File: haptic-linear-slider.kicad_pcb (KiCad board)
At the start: 2 copper layers, 130.5 x 46 mm, 67 parts, among them J1 EXT_CTRL, J2 SWD, J3 USB_C_Receptacle_USB2.0_16P, J4 TBC05-02-1-G-G, SW1 SW_Reset, SW2 SW_Boot, U1 STM32C071KBT6, U2 PSM01-081A-103B2, U3 USBLC6-2SC6, U4 DRV8876PWPR, U5 DIO54335TST6, U6 TLV61048DBVR, U7 TPS22918DBVR

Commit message: review of main components
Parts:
- removed C21: 47u, Capacitor_SMD:C_1210_3225Metric_Pad1.33x2.70mm_HandSolder
- added R10: 1k, Resistor_SMD:R_0805_2012Metric_Pad1.20x1.40mm_HandSolder, F.Cu at (316.2, 214.5)
- added R27: 10k, Resistor_SMD:R_0805_2012Metric_Pad1.20x1.40mm_HandSolder, F.Cu at (226.5, 212.7)
- C9: value 1u -> 10u; footprint Capacitor_SMD:C_0805_2012Metric_Pad1.18x1.45mm_HandSolder -> Capacitor_SMD:C_1210_3225Metric_Pad1.33x2.70mm_HandSolder
- moved D4 27.7 mm to (278.5, 217.6), turned to 180 degrees
- moved R26 21.8 mm to (274.2, 217.6), turned to 0 degrees
- moved C1 14.6 mm to (302.6, 225.9), turned to 0 degrees
- moved C2 13.9 mm to (302.6, 229.5)
- moved C38 13.7 mm to (234.1, 227.8), turned to 90 degrees
- moved C9 10.9 mm to (317.0, 221.1), turned to -90 degrees
- moved D1 10.6 mm to (302.6, 222.8)
- moved R1 10.4 mm to (307.8, 232.4), turned to 90 degrees
- moved C33 8.78 mm to (228.5, 215.2), turned to 0 degrees
- moved U6 7.59 mm to (309.1, 224.7)
- moved R2 7.30 mm to (308.8, 229.2), turned to 0 degrees
- moved J1 6.39 mm to (237.7, 235.1)
- moved C6 6.32 mm to (291.2, 223.2)
- moved U5 5.80 mm to (291.1, 226.6), turned to -90 degrees
- moved R14 5.39 mm to (231.3, 219.0), turned to 180 degrees
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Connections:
- net /LS_CT renamed Net-(U7-CT)
- net /LS_ON renamed Net-(U7-ON)
- net /MOTOR_OUT1 renamed Net-(U4-OUT1)
- net /MOTOR_OUT2 renamed Net-(U4-OUT2)
- C33 pad 1: /MOTOR_VREF_PWM -> Net-(U4-VREF)
- R15 pad 1: /MOTOR_VREF_PWM -> Net-(U4-VREF)
- U4 pad 5: /MOTOR_VREF_PWM -> Net-(U4-VREF)
- U7 pad 5: unconnected-(U7-QOD-Pad5) -> Net-(U7-QOD)
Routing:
- net /CC_SENSE: track 152.9 -> 110.9 mm
- net /POT_WIPER1: track 114.9 -> 78.1 mm, vias 0 -> 1
- net /POT_WIPER2: track 105.6 -> 71.1 mm, vias 0 -> 1
- net Net-(U4-VREF): track 0.00 -> 19.4 mm
- net /MOTOR_VREF_PWM: track 77.0 -> 61.4 mm
- net +10V: track 111.0 -> 121.3 mm
- net Net-(U5-BS): track 2.09 -> 11.4 mm
- net /BOOST_SW: track 9.02 -> 0.00 mm
- net GND: track 82.0 -> 90.3 mm, vias 47 -> 51
- net /TOUCH_SENSE: track 46.4 -> 40.6 mm
- net +5V: track 181.3 -> 175.8 mm
- net Net-(U4-OUT1): track 20.8 -> 15.4 mm
- net /MOTOR_IPROPI: track 64.8 -> 60.4 mm
- net Net-(U4-OUT2): track 17.0 -> 12.6 mm
- net /BUCK_SW: track 8.65 -> 12.5 mm
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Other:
- board text removed: "7 VREF 8 IPRO 9 W1 10 W2 11 TCH 12 CC 13/14 GND"
- board text removed: "J1 EXT CTRL 1 3V3 2 5V 3 IN1 4 IN2 5 SLP 6 FLT"

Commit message: ready to order
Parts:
- removed R6: 1k, Resistor_SMD:R_0805_2012Metric_Pad1.20x1.40mm_HandSolder
- removed SW1: SW_Reset, _Footprints:434133025816
- C17: value 3n3 -> 22n
- J2: footprint Connector_PinHeader_2.54mm:PinHeader_1x04_P2.54mm_Vertical -> Connector_PinHeader_2.54mm:PinHeader_1x05_P2.54mm_Vertical
- U1: value STM32C071KBT6 -> STM32C071KBT3
- moved C2 73.8 mm to (228.9, 235.3), turned to -90 degrees
- moved C10 8.96 mm to (258.9, 229.3), turned to 0 degrees
- moved C38 2.71 mm to (233.5, 225.2), turned to 0 degrees
- moved D3 0.94 mm to (261.7, 202.8), turned to 0 degrees
- moved D2 0.91 mm to (265.9, 202.8), turned to 180 degrees
- moved C36 0.88 mm to (222.6, 232.9)
- moved C37 0.26 mm to (229.2, 231.5)
- moved C11 0.05 mm to (321.6, 215.3)
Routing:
- net GND: track 90.3 -> 60.5 mm, vias 51 -> 47
- net /NRST: track 42.6 -> 34.9 mm
- net Net-(R6-Pad1): track 6.78 -> 0.00 mm
- net Net-(U2-T): track 87.3 -> 93.0 mm
- net /+5V_MOT: track 20.4 -> 15.8 mm
- net +10V: track 121.3 -> 118.8 mm
- net Net-(D3-A): track 2.23 -> 3.11 mm
- net Net-(D2-A): track 2.23 -> 3.09 mm
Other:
- board text added: "+"
- board text added: "-"
- board text added: "3V3"
- board text added: "5V"
- board text added: "CC_SENSE"
- board text added: "GND"
- board text added: "M_IN1"
- board text added: "M_IN2"
- board text added: "M_IPROPI"
- board text added: "M_VREF"
- board text added: "M_~{FAULT}"
- board text added: "M_~{SLEEP}"
- board text added: "NRST"
- board text added: "P_WIPER1"
- board text added: "P_WIPER2"
- board text added: "SWCLK"
- board text added: "SWD"
- board text added: "TC_SENSE"

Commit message: logo
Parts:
- added TP1: TestPoint, TestPoint:TestPoint_THTPad_D1.0mm_Drill0.5mm, F.Cu at (304.2, 231.6)
- moved C23 0.24 mm to (253.8, 214.5)
- moved C22 0.22 mm to (256.3, 214.5)
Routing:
- net /NRST: track 34.9 -> 32.4 mm
- net +10V: track 118.8 -> 120.9 mm
- net GND: track 60.5 -> 61.8 mm
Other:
- board text added: "haptic-linear-slider v1.0.1"

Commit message: v.1.1.0: differential pair size and JCLPCB rules
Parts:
- moved J2 6.54 mm to (289.1, 212.7), turned to 180 degrees
- moved C15 4.55 mm to (281.0, 206.8)
- moved R8 4.55 mm to (278.5, 206.8)
- moved R9 4.55 mm to (283.4, 206.8)
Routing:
- net Net-(J2-Pin_4): track 17.0 -> 5.95 mm, vias 1 -> 0
- net /SWCLK: track 36.8 -> 26.1 mm, vias 1 -> 0
- net /SWD: track 28.9 -> 22.6 mm, vias 1 -> 0
- net /NRST: track 32.4 -> 27.9 mm
- net /USB_D+: track 83.4 -> 84.7 mm
- net /USB_D-: track 84.9 -> 85.6 mm
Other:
- board text added: "haptic-linear-slider v1.1.0"
- board text removed: "haptic-linear-slider v1.0.1"

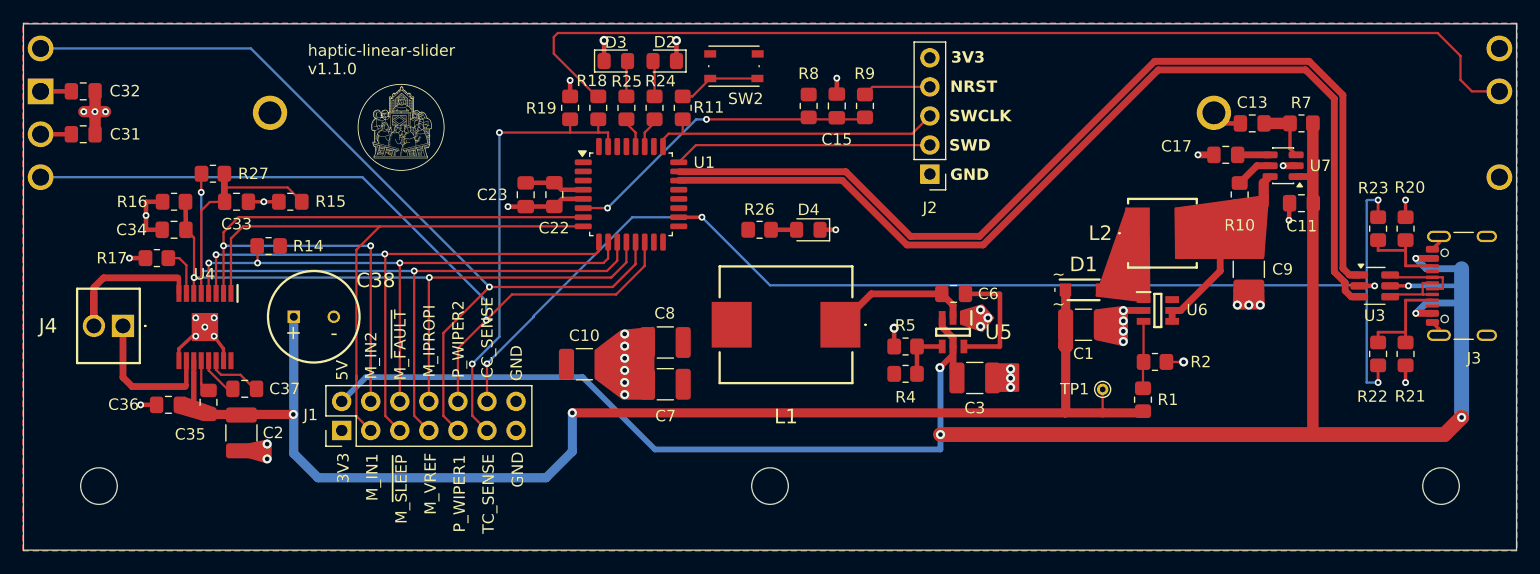
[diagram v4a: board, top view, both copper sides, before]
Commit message: Aggiunto connettore J5
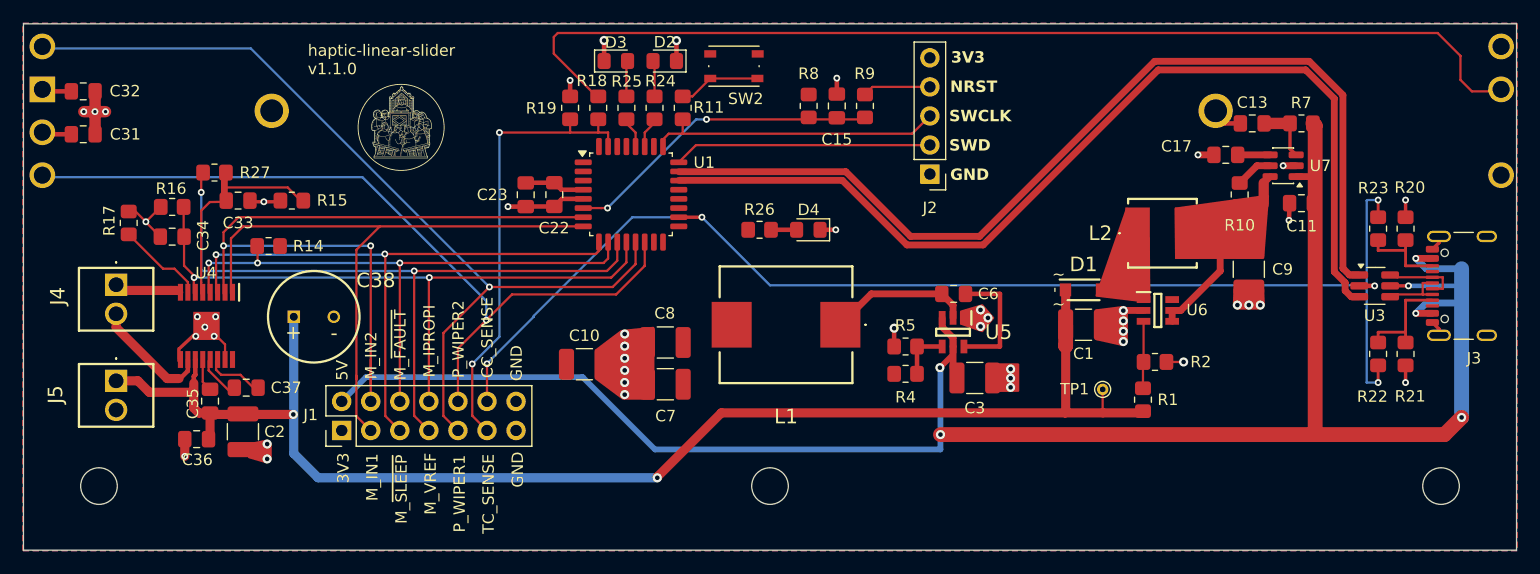
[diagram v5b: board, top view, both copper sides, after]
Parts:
- added J5: TBC05-02-1-G-G, _Footprints:TBC05021GG, F.Cu at (218.0, 230.8)
- moved R17 3.94 mm to (219.1, 217.0), turned to 90 degrees
- moved C36 3.88 mm to (225.0, 235.9)
- moved J4 3.65 mm to (218.0, 222.4), turned to -90 degrees
- moved C34 0.62 mm to (222.9, 218.2)
- moved R16 0.48 mm to (222.9, 215.6)
- moved U2 0.23 mm to (211.6, 205.3)
- moved C35 0.17 mm to (226.2, 232.6)
- moved R15 0.17 mm to (233.4, 215.0)
- moved C2 0.17 mm to (229.1, 235.2)
- moved U4 0.17 mm to (225.9, 226.0)
- moved C33 0.17 mm to (228.7, 215.0)
- moved C37 0.17 mm to (229.4, 231.4)
- moved R27 0.17 mm to (226.6, 212.6)
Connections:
- J4 pad 1: Net-(U4-OUT2) -> Net-(U4-OUT1)
- J4 pad 2: Net-(U4-OUT1) -> Net-(U4-OUT2)
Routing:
- net Net-(U4-OUT1): track 15.4 -> 5.90 mm
- net +10V: track 120.9 -> 130.2 mm
- net Net-(U4-IMODE): track 4.38 -> 7.79 mm
- net Net-(U4-OUT2): track 12.6 -> 10.5 mm
- net /MOTOR_IPROPI: track 60.4 -> 59.0 mm
- net GND: track 61.8 -> 62.3 mm, vias 47 -> 46
